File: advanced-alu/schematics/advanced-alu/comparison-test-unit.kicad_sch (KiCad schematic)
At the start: 10 parts

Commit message: returned temp registr to being 8-bit
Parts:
- gave numbers to parts that had none: 10
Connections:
- net HI_TMP_0 renamed TMP_0
- net HI_TMP_1 renamed TMP_1
- net HI_TMP_2 renamed TMP_2
- net HI_TMP_3 renamed TMP_3
- net HI_TMP_4 renamed TMP_4
- net HI_TMP_5 renamed TMP_5
- net HI_TMP_6 renamed TMP_6
- net HI_TMP_7 renamed TMP_7
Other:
- note added: "When CPMs is HIGH, the E(quals) flag is set when data bus and TMP values are equal, and the O(verflow) flag is set when value in TMP register is greater than the value on the data bus. Otherwise, Z(ero) flag is set when data bus value is zero."
- note removed: "When CPMs is HIGH, the E(quals) flag is set when data bus and HI_TMP values are equal, and the O(verflow) flag is set when value in HI_TMP register is greater than the value on the data bus. Otherwise, Z(ero) flag is set when data bus value is zero."
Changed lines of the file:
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@@
     (effects (font (size 2 2)) (justify left bottom))
   )
-  (text "When CPMs is HIGH, the E(quals) flag is set when data bus and HI_TMP\nvalues are equal, and the O(verflow) flag is set when value in\nHI_TMP register is greater than the value on the data bus.\nOtherwise, Z(ero) flag is set when data bus value is zero."
+  (text "When CPMs is HIGH, the E(quals) flag is set when data bus and TMP\nvalues are equal, and the O(verflow) flag is set when value in\nTMP register is greater than the value on the data bus.\nOtherwise, Z(ero) flag is set when data bus value is zero."
     (at 170.942 30.226 0)
     (effects (font (size 2 2)) (justify left bottom))
   )
-  (label "HI_TMP_7" (at 58.42 49.53 0)
+  (label "TMP_7" (at 58.42 49.53 0)
     (effects (font (size 1.27 1.27)) (justify left bottom))
   )
@@
     (effects (font (size 1.27 1.27)) (justify left bottom))
   )
-  (label "HI_TMP_2" (at 120.65 163.83 0)
+  (label "TMP_2" (at 120.65 163.83 0)
     (effects (font (size 1.27 1.27)) (justify left bottom))
   )
@@
     (effects (font (size 1.27 1.27)) (justify left bottom))
   )
-  (label "HI_TMP_1" (at 120.65 161.29 0)
-    (effects (font (size 1.27 1.27)) (justify left bottom))
-  )
-  (label "HI_TMP_6" (at 58.42 46.99 0)
+  (label "TMP_1" (at 120.65 161.29 0)
+    (effects (font (size 1.27 1.27)) (justify left bottom))
+  )
+  (label "TMP_6" (at 58.42 46.99 0)
     (effects (font (size 1.27 1.27)) (justify left bottom))
   )
@@
     (effects (font (size 1.27 1.27)) (justify left bottom))
   )
-  (label "HI_TMP_5" (at 58.42 44.45 0)
-    (effects (font (size 1.27 1.27)) (justify left bottom))
-  )
-  (label "HI_TMP_0" (at 120.65 158.75 0)
-    (effects (font (size 1.27 1.27)) (justify left bottom))
-  )
-  (label "HI_TMP_0" (at 58.42 31.75 0)
-    (effects (font (size 1.27 1.27)) (justify left bottom))
-  )
-  (label "HI_TMP_2" (at 58.42 36.83 0)
-    (effects (font (size 1.27 1.27)) (justify left bottom))
-  )
-  (label "HI_TMP_4" (at 58.42 41.91 0)
+  (label "TMP_5" (at 58.42 44.45 0)
+    (effects (font (size 1.27 1.27)) (justify left bottom))
+  )
+  (label "TMP_0" (at 120.65 158.75 0)
+    (effects (font (size 1.27 1.27)) (justify left bottom))
+  )
+  (label "TMP_0" (at 58.42 31.75 0)
+    (effects (font (size 1.27 1.27)) (justify left bottom))
+  )
+  (label "TMP_2" (at 58.42 36.83 0)
+    (effects (font (size 1.27 1.27)) (justify left bottom))
+  )
+  (label "TMP_4" (at 58.42 41.91 0)
     (effects (font (size 1.27 1.27)) (justify left bottom))
   )
@@
     (effects (font (size 1.27 1.27)) (justify left bottom))
   )
-  (label "HI_TMP_1" (at 58.42 34.29 0)
+  (label "TMP_1" (at 58.42 34.29 0)
     (effects (font (size 1.27 1.27)) (justify left bottom))
   )
@@
     (effects (font (size 1.27 1.27)) (justify left bottom))
   )
-  (label "HI_TMP_3" (at 58.42 39.37 0)
-    (effects (font (size 1.27 1.27)) (justify left bottom))
-  )
-  (hierarchical_label "HI_TMP_[0..7]" (shape input) (at 31.115 76.835 180)
+  (label "TMP_3" (at 58.42 39.37 0)
+    (effects (font (size 1.27 1.27)) (justify left bottom))
+  )
+  (hierarchical_label "TMP_[0..7]" (shape input) (at 31.115 76.835 180)
     (effects (font (size 1.27 1.27)) (justify right))
   )
@@
   (symbol (lib_id "74xx_IEEE:74LS682") (at 143.51 93.98 0) (unit 1)
     (in_bom yes) (on_board yes)
-    (property "Reference" "U?" (id 0) (at 151.765 114.935 0))
+    (property "Reference" "U20" (id 0) (at 151.765 114.935 0))
     (property "Value" "74LS682" (id 1) (at 144.78 93.98 0))
     (property "Footprint" "" (id 2) (at 143.51 93.98 0)
@@
   (symbol (lib_id "Device:R_Network08_US") (at 140.97 39.37 270) (mirror x) (unit 1)
     (in_bom yes) (on_board yes) (fields_autoplaced)
-    (property "Reference" "RN?" (id 0) (at 140.716 26.5135 90))
+    (property "Reference" "RN2" (id 0) (at 140.716 26.5135 90))
     (property "Value" "10K Ω" (id 1) (at 140.716 29.2886 90))
     (property "Footprint" "Resistor_THT:R_Array_SIP9" (id 2) (at 140.97 27.305 90)
@@
   (symbol (lib_id "74xx:74LS08") (at 208.915 49.53 0) (unit 1)
     (in_bom yes) (on_board yes) (fields_autoplaced)
-    (property "Reference" "U?" (id 0) (at 208.915 42.0202 0))
+    (property "Reference" "U23" (id 0) (at 208.915 42.0202 0))
     (property "Value" "74LS08" (id 1) (at 208.915 44.5571 0))
     (property "Footprint" "" (id 2) (at 208.915 49.53 0)
@@
   (symbol (lib_id "power:GND") (at 148.59 49.53 0) (unit 1)
     (in_bom yes) (on_board yes) (fields_autoplaced)
-    (property "Reference" "#PWR?" (id 0) (at 148.59 55.88 0)
+    (property "Reference" "#PWR028" (id 0) (at 148.59 55.88 0)
       (effects (font (size 1.27 1.27)) hide)
     )
@@
   (symbol (lib_id "74xx:74LS04") (at 168.275 82.55 0) (unit 1)
     (in_bom yes) (on_board yes) (fields_autoplaced)
-    (property "Reference" "U?" (id 0) (at 168.275 74.7735 0))
+    (property "Reference" "U22" (id 0) (at 168.275 74.7735 0))
     (property "Value" "74LS04" (id 1) (at 168.275 77.5486 0))
     (property "Footprint" "" (id 2) (at 168.275 82.55 0)
@@
   (symbol (lib_id "74xx:74LS151") (at 144.78 151.13 0) (unit 1)
     (in_bom yes) (on_board yes)
-    (property "Reference" "U?" (id 0) (at 153.67 170.815 0)
+    (property "Reference" "U21" (id 0) (at 153.67 170.815 0)
       (effects (font (size 1.27 1.27)) (justify left))
     )
@@
   (symbol (lib_id "power:GND") (at 82.55 132.715 0) (unit 1)
     (in_bom yes) (on_board yes) (fields_autoplaced)
-    (property "Reference" "#PWR?" (id 0) (at 82.55 139.065 0)
+    (property "Reference" "#PWR025" (id 0) (at 82.55 139.065 0)
       (effects (font (size 1.27 1.27)) hide)
     )
@@
   (symbol (lib_id "power:GND") (at 144.78 176.53 0) (unit 1)
     (in_bom yes) (on_board yes) (fields_autoplaced)
-    (property "Reference" "#PWR?" (id 0) (at 144.78 182.88 0)
+    (property "Reference" "#PWR027" (id 0) (at 144.78 182.88 0)
       (effects (font (size 1.27 1.27)) hide)
     )
@@
   (symbol (lib_id "74xx:74LS245") (at 82.55 44.45 0) (unit 1)
     (in_bom yes) (on_board yes)
-    (property "Reference" "U?" (id 0) (at 87.63 27.94 0)
+    (property "Reference" "U18" (id 0) (at 87.63 27.94 0)
       (effects (font (size 1.27 1.27)) (justify left))
     )
@@
   (symbol (lib_id "74xx:74LS08") (at 208.915 66.04 0) (unit 2)
     (in_bom yes) (on_board yes) (fields_autoplaced)
-    (property "Reference" "U?" (id 0) (at 208.915 58.5302 0))
+    (property "Reference" "U8" (id 0) (at 208.915 58.5302 0))
     (property "Value" "74LS08" (id 1) (at 208.915 61.0671 0))
     (property "Footprint" "" (id 2) (at 208.915 66.04 0)
@@
   (symbol (lib_id "74xx:74LS245") (at 82.55 109.22 0) (unit 1)
     (in_bom yes) (on_board yes)
-    (property "Reference" "U?" (id 0) (at 87.63 92.71 0)
+    (property "Reference" "U19" (id 0) (at 87.63 92.71 0)
       (effects (font (size 1.27 1.27)) (justify left))
     )
@@
   (symbol (lib_id "74xx:74LS04") (at 186.055 46.99 0) (unit 3)
     (in_bom yes) (on_board yes) (fields_autoplaced)
-    (property "Reference" "U?" (id 0) (at 186.055 39.4802 0))
+    (property "Reference" "U1" (id 0) (at 186.055 39.4802 0))
     (property "Value" "74LS04" (id 1) (at 186.055 42.0171 0))
     (property "Footprint" "" (id 2) (at 186.055 46.99 0)
@@
   (symbol (lib_id "power:VCC") (at 82.55 88.9 0) (unit 1)
     (in_bom yes) (on_board yes) (fields_autoplaced)
-    (property "Reference" "#PWR?" (id 0) (at 82.55 92.71 0)
+    (property "Reference" "#PWR024" (id 0) (at 82.55 92.71 0)
       (effects (font (size 1.27 1.27)) hide)
     )
@@
   (symbol (lib_id "power:VCC") (at 144.78 127 0) (unit 1)
     (in_bom yes) (on_board yes) (fields_autoplaced)
-    (property "Reference" "#PWR?" (id 0) (at 144.78 130.81 0)
+    (property "Reference" "#PWR026" (id 0) (at 144.78 130.81 0)
       (effects (font (size 1.27 1.27)) hide)
     )
@@
   (symbol (lib_id "power:GND") (at 82.55 64.77 0) (unit 1)
     (in_bom yes) (on_board yes) (fields_autoplaced)
-    (property "Reference" "#PWR?" (id 0) (at 82.55 71.12 0)
+    (property "Reference" "#PWR023" (id 0) (at 82.55 71.12 0)
       (effects (font (size 1.27 1.27)) hide)
     )
@@
   (symbol (lib_id "74xx:74LS04") (at 168.275 105.41 0) (unit 2)
     (in_bom yes) (on_board yes) (fields_autoplaced)
-    (property "Reference" "U?" (id 0) (at 168.275 97.6335 0))
+    (property "Reference" "U4" (id 0) (at 168.275 97.6335 0))
     (property "Value" "74LS04" (id 1) (at 168.275 100.4086 0))
     (property "Footprint" "" (id 2) (at 168.275 105.41 0)
@@
   (symbol (lib_id "power:VCC") (at 82.55 24.13 0) (unit 1)
     (in_bom yes) (on_board yes) (fields_autoplaced)
-    (property "Reference" "#PWR?" (id 0) (at 82.55 27.94 0)
-      (effects (font (size 1.27 1.27)) hide)
-    )
+    (property "Reference" "#PWR022" (id 0) (at 82.55 27.94 0)
+      (effects (font (size 1.27 1.27)) hide)
+    )

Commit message: tweaked design and updated documentation
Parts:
- added U?: (no value), symbol 74xx:74LS04
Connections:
- net CMPs: now also U?.9; no longer U18.19 (CE)
- new net: U18.19 (CE), U?.8
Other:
- note added: "In BIT mode, the Z(ero) flag is set if if the data bus bit identified by TMP_[0..2] is equal to zero."
- note removed: "In BIT mode, the Z(ero) flag is set if if the data bus bit identified by HI_TMP_[0..2] is equal to zero."
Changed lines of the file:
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@@
   (junction (at 114.3 46.99) (diameter 0) (color 0 0 0 0)
   )
-  (junction (at 59.69 57.15) (diameter 0) (color 0 0 0 0)
-  )
   (junction (at 121.92 39.37) (diameter 0) (color 0 0 0 0)
   )
@@
   )
   (junction (at 127 34.29) (diameter 0) (color 0 0 0 0)
+  )
+  (junction (at 36.068 57.15) (diameter 0) (color 0 0 0 0)
   )
   (junction (at 114.3 114.3) (diameter 0) (color 0 0 0 0)
@@
     (stroke (width 0) (type default) (color 0 0 0 0))
   )
-  (wire (pts (xy 59.69 57.15) (xy 69.85 57.15))
-    (stroke (width 0) (type default) (color 0 0 0 0))
-  )
   (wire (pts (xy 123.825 140.97) (xy 132.08 140.97))
     (stroke (width 0) (type default) (color 0 0 0 0))
@@
     (stroke (width 0) (type default) (color 0 0 0 0))
   )
+  (wire (pts (xy 67.818 57.15) (xy 69.85 57.15))
+    (stroke (width 0) (type default) (color 0 0 0 0))
+  )
   (wire (pts (xy 124.46 36.83) (xy 124.46 78.74))
     (stroke (width 0) (type default) (color 0 0 0 0))
@@
     (stroke (width 0) (type default) (color 0 0 0 0))
   )
-  (wire (pts (xy 59.69 57.15) (xy 59.69 73.025))
-    (stroke (width 0) (type default) (color 0 0 0 0))
-  )
   (wire (pts (xy 82.55 129.54) (xy 82.55 132.715))
     (stroke (width 0) (type default) (color 0 0 0 0))
@@
     (stroke (width 0) (type default) (color 0 0 0 0))
   )
+  (wire (pts (xy 36.068 73.025) (xy 36.068 57.15))
+    (stroke (width 0) (type default) (color 0 0 0 0))
+  )
   (wire (pts (xy 111.125 158.75) (xy 132.08 158.75))
     (stroke (width 0) (type default) (color 0 0 0 0))
@@
     (stroke (width 0) (type default) (color 0 0 0 0))
   )
-  (wire (pts (xy 31.115 57.15) (xy 59.69 57.15))
+  (wire (pts (xy 31.115 57.15) (xy 36.068 57.15))
     (stroke (width 0) (type default) (color 0 0 0 0))
   )
@@
     (stroke (width 0) (type default) (color 0 0 0 0))
   )
-  (wire (pts (xy 59.69 73.025) (xy 101.6 73.025))
+  (wire (pts (xy 36.068 73.025) (xy 101.6 73.025))
     (stroke (width 0) (type default) (color 0 0 0 0))
   )
@@
     (stroke (width 0) (type default) (color 0 0 0 0))
   )
+  (wire (pts (xy 36.068 57.15) (xy 52.578 57.15))
+    (stroke (width 0) (type default) (color 0 0 0 0))
+  )
   (wire (pts (xy 111.76 49.53) (xy 111.76 91.44))
     (stroke (width 0) (type default) (color 0 0 0 0))
@@
     (stroke (width 0) (type default) (color 0 0 0 0))
   )
-  (text "In BIT mode, the Z(ero) flag is set if if the data bus bit\nidentified by HI_TMP_[0..2] is equal to zero."
+  (text "In BIT mode, the Z(ero) flag is set if if the data bus bit\nidentified by TMP_[0..2] is equal to zero."
     (at 181.61 133.985 0)
     (effects (font (size 2 2)) (justify left bottom))
@@
     (pin "9")
   )
+  (symbol (lib_id "74xx:74LS04") (at 60.198 57.15 0) (unit 4)
+    (in_bom yes) (on_board yes)
+    (property "Reference" "U?" (id 0) (at 62.484 64.516 0))
+    (property "Value" "" (id 1) (at 60.706 62.23 0))
+    (property "Footprint" "" (id 2) (at 60.198 57.15 0)
+      (effects (font (size 1.27 1.27)) hide)
+    )
+    (property "Datasheet" "http://www.ti.com/lit/gpn/sn74LS04" (id 3) (at 60.198 57.15 0)
+      (effects (font (size 1.27 1.27)) hide)
+    )
+    (pin "1")
+    (pin "2")
+    (pin "3")
+    (pin "4")
+    (pin "5")
+    (pin "6")
+    (pin "8")
+    (pin "9")
+    (pin "10")
+    (pin "11")
+    (pin "12")
+    (pin "13")
+    (pin "14")
+    (pin "7")
+  )
   (symbol (lib_id "74xx:74LS08") (at 208.915 66.04 0) (unit 2)

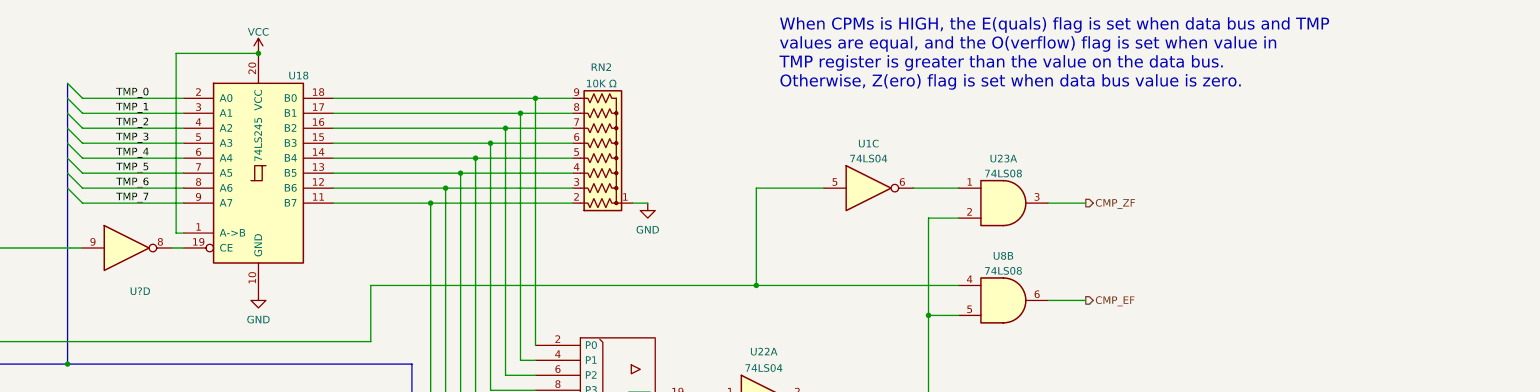
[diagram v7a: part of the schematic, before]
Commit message: improvements to how carry is handled
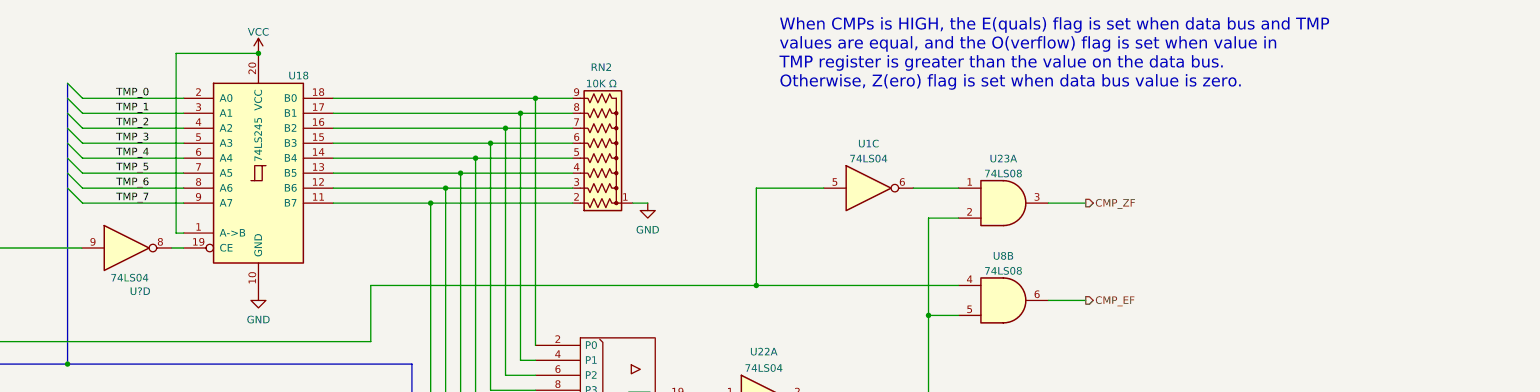
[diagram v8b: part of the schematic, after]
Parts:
- U?: value (none) -> 74LS04
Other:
- note added: "When CMPs is HIGH, the E(quals) flag is set when data bus and TMP values are equal, and the O(verflow) flag is set when value in TMP register is greater than the value on the data bus. Otherwise, Z(ero) flag is set when data bus value is zero."
- note removed: "When CPMs is HIGH, the E(quals) flag is set when data bus and TMP values are equal, and the O(verflow) flag is set when value in TMP register is greater than the value on the data bus. Otherwise, Z(ero) flag is set when data bus value is zero."
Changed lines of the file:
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@@
     (effects (font (size 2 2)) (justify left bottom))
   )
-  (text "When CPMs is HIGH, the E(quals) flag is set when data bus and TMP\nvalues are equal, and the O(verflow) flag is set when value in\nTMP register is greater than the value on the data bus.\nOtherwise, Z(ero) flag is set when data bus value is zero."
+  (text "When CMPs is HIGH, the E(quals) flag is set when data bus and TMP\nvalues are equal, and the O(verflow) flag is set when value in\nTMP register is greater than the value on the data bus.\nOtherwise, Z(ero) flag is set when data bus value is zero."
     (at 170.942 30.226 0)
     (effects (font (size 2 2)) (justify left bottom))
@@
     (pin "2")
     (pin "3")
+    (pin "4")
+    (pin "5")
+    (pin "6")
+    (pin "10")
+    (pin "8")
+    (pin "9")
+    (pin "11")
+    (pin "12")
+    (pin "13")
+    (pin "14")
+    (pin "7")
   )
   (symbol (lib_id "power:GND") (at 148.59 49.53 0) (unit 1)
@@
     (pin "1")
     (pin "2")
+    (pin "3")
+    (pin "4")
+    (pin "5")
+    (pin "6")
+    (pin "8")
+    (pin "9")
+    (pin "10")
+    (pin "11")
+    (pin "12")
+    (pin "13")
+    (pin "14")
+    (pin "7")
   )
   (symbol (lib_id "74xx:74LS151") (at 144.78 151.13 0) (unit 1)
@@
     (in_bom yes) (on_board yes)
     (property "Reference" "U?" (id 0) (at 62.484 64.516 0))
-    (property "Value" "" (id 1) (at 60.706 62.23 0))
+    (property "Value" "74LS04" (id 1) (at 60.706 62.23 0))
     (property "Footprint" "" (id 2) (at 60.198 57.15 0)
       (effects (font (size 1.27 1.27)) hide)
@@
       (effects (font (size 1.27 1.27)) hide)
     )
-    (pin "8")
-    (pin "9")
+    (pin "1")
+    (pin "2")
+    (pin "3")
+    (pin "4")
+    (pin "5")
+    (pin "6")
+    (pin "8")
+    (pin "9")
+    (pin "10")
+    (pin "11")
+    (pin "12")
+    (pin "13")
+    (pin "14")
+    (pin "7")
   )
   (symbol (lib_id "74xx:74LS08") (at 208.915 66.04 0) (unit 2)
@@
       (effects (font (size 1.27 1.27)) hide)
     )
-    (pin "4")
-    (pin "5")
-    (pin "6")
+    (pin "1")
+    (pin "2")
+    (pin "3")
+    (pin "4")
+    (pin "5")
+    (pin "6")
+    (pin "10")
+    (pin "8")
+    (pin "9")
+    (pin "11")
+    (pin "12")
+    (pin "13")
+    (pin "14")
+    (pin "7")
   )
   (symbol (lib_id "74xx:74LS245") (at 82.55 109.22 0) (unit 1)
@@
       (effects (font (size 1.27 1.27)) hide)
     )
-    (pin "5")
-    (pin "6")
+    (pin "1")
+    (pin "2")
+    (pin "3")
+    (pin "4")
+    (pin "5")
+    (pin "6")
+    (pin "8")
+    (pin "9")
+    (pin "10")
+    (pin "11")
+    (pin "12")
+    (pin "13")
+    (pin "14")
+    (pin "7")
   )
   (symbol (lib_id "power:VCC") (at 82.55 88.9 0) (unit 1)
@@
       (effects (font (size 1.27 1.27)) hide)
     )
-    (pin "3")
-    (pin "4")
+    (pin "1")
+    (pin "2")
+    (pin "3")
+    (pin "4")
+    (pin "5")
+    (pin "6")
+    (pin "8")
+    (pin "9")
+    (pin "10")
+    (pin "11")
+    (pin "12")
+    (pin "13")
+    (pin "14")
+    (pin "7")
   )
   (symbol (lib_id "power:VCC") (at 82.55 24.13 0) (unit 1)
